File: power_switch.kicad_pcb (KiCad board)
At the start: 2 copper layers, 69 parts, among them P1 CONN_2, P10 CONN_2, P11 CONN_2, P12 CONN_2, P13 CONN_02X01, P2 CONN_2, P20 CONN_2, P3 CONN_2, P4 CONN_2, P5 CONN_2, P6 CONN_02X01, P7 CONN_02X01, P8 CONN_02X01, P9 CONN_2, Q1 2N7000, Q2 IRF9540, Q3 IRF9540, Q4 Q_NMOS_DGS, Q5 IRF9540, Q6 2N7000, U1 LM358

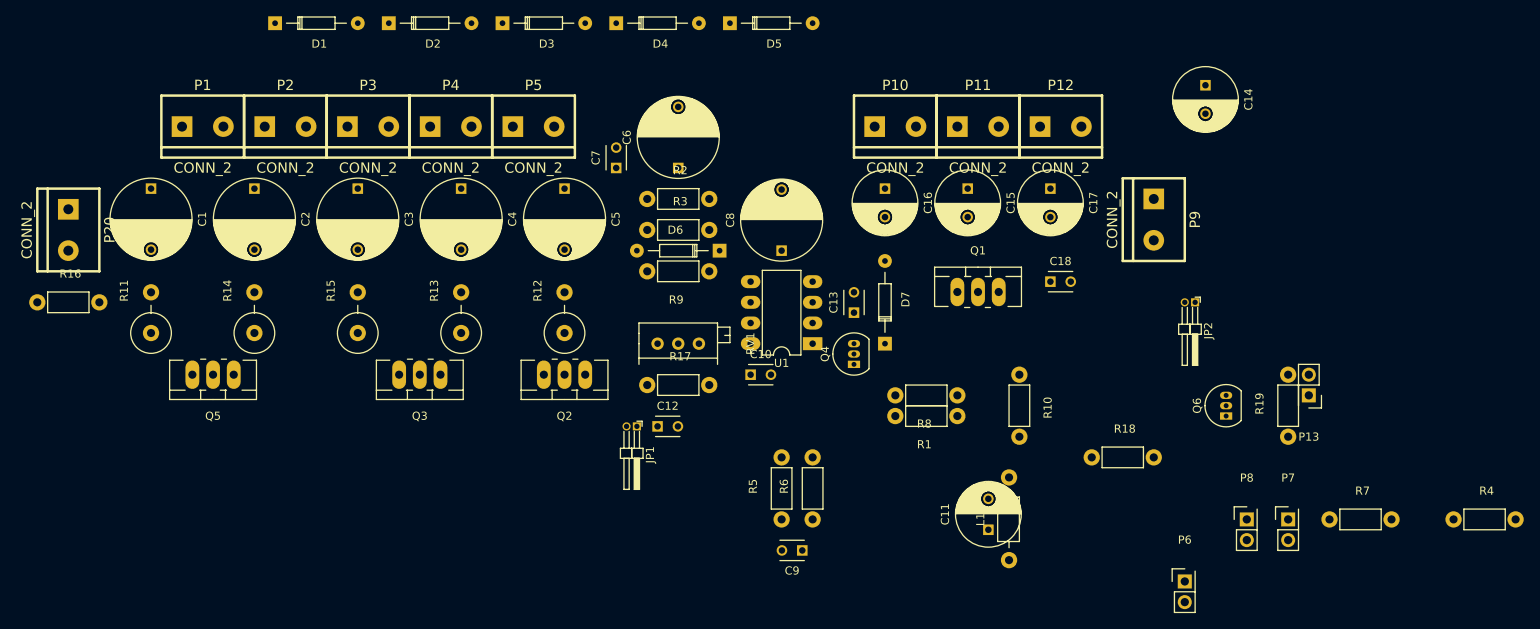
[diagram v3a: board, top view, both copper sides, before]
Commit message: powerswitch with tracks
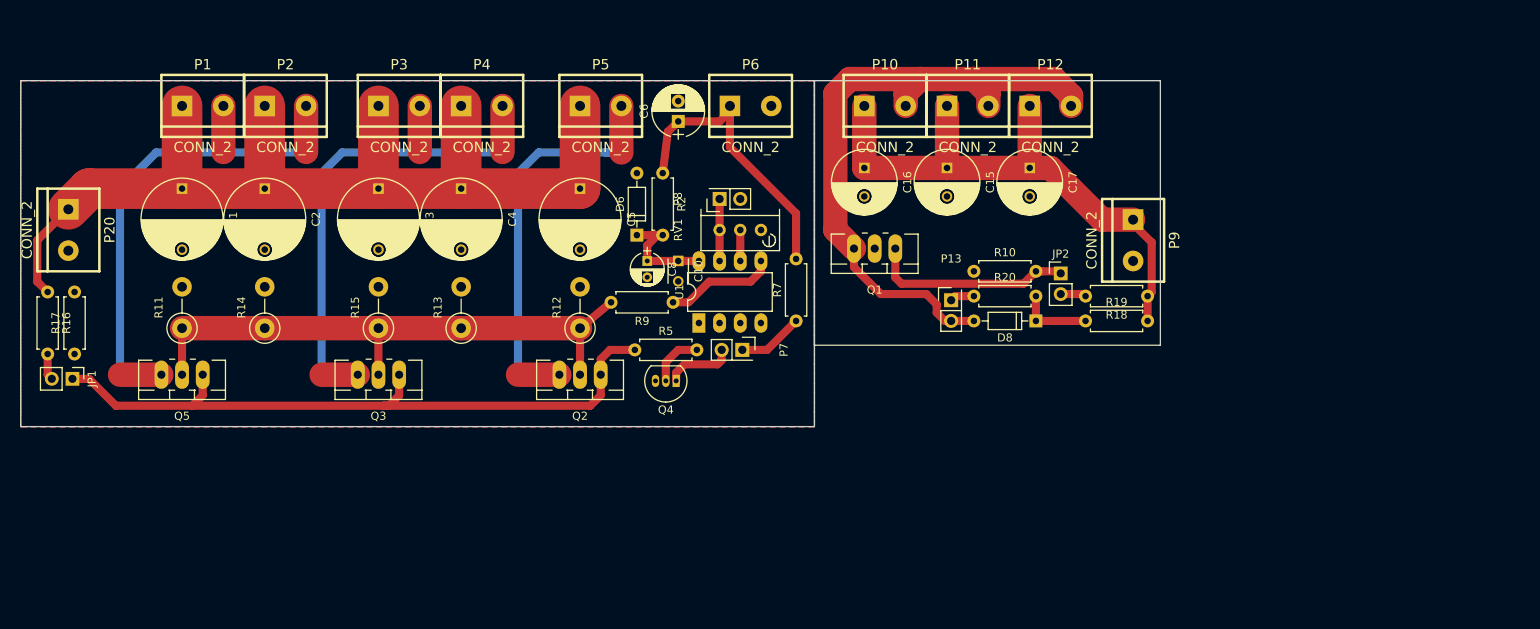
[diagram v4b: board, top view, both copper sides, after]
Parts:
- removed C11: 10uF, Capacitors_ThroughHole:C_Radial_D8_L13_P3.8
- removed C12, C18, C7, C9: 100n, Capacitors_ThroughHole:C_Disc_D3_P2.5
- removed C13: C, Capacitors_ThroughHole:C_Disc_D3_P2.5
- removed C14: 10uF, Capacitors_ThroughHole:C_Radial_D8_L11.5_P3.5
- removed D1, D2, D3, D4, D5: D, Diodes_ThroughHole:Diode_DO-35_SOD27_Horizontal_RM10
- removed D7: 1N4001, Diodes_ThroughHole:Diode_DO-35_SOD27_Horizontal_RM10
- removed L1: 50uH, Choke_Axial_ThroughHole:Choke_Horizontal_RM10mm
- removed Q6: 2N7000, TO_SOT_Packages_THT:TO-92_Inline_Narrow_Oval
- removed R1, R3, R6, R8: R, Resistors_ThroughHole:Resistor_Horizontal_RM7mm
- removed R4: 220R, Resistors_ThroughHole:Resistor_Horizontal_RM7mm
- added D8: 5v6, Diodes_ThroughHole:D_DO-35_SOD27_P7.62mm_Horizontal, F.Cu at (172.2, 64.5)
- added R20: 220R, Resistors_ThroughHole:R_Axial_DIN0207_L6.3mm_D2.5mm_P7.62mm_Horizontal, F.Cu at (164.6, 61.5)
- C6: footprint Capacitors_ThroughHole:C_Radial_D10_L20_P7.5 -> Capacitors_ThroughHole:CP_Radial_D6.3mm_P2.50mm
- C8: footprint Capacitors_ThroughHole:C_Radial_D10_L20_P7.5 -> Capacitors_ThroughHole:CP_Radial_D4.0mm_P2.00mm
- D6: footprint Diodes_ThroughHole:Diode_DO-35_SOD27_Horizontal_RM10 -> Diodes_ThroughHole:D_DO-35_SOD27_P7.62mm_Horizontal
- JP1, JP2: footprint Pin_Headers:Pin_Header_Angled_1x02_Pitch1.27mm -> Pin_Headers:Pin_Header_Straight_1x02_Pitch2.54mm
- P6: value CONN_02X01 -> CONN_2; footprint Socket_Strips:Socket_Strip_Straight_2x01 -> borniers:bornier2_V
- Q1: value 2N7000 -> IRF9540
- R10, R16, R17, R18, R19, R2, R5, R7, R9: footprint Resistors_ThroughHole:Resistor_Horizontal_RM7mm -> Resistors_ThroughHole:R_Axial_DIN0207_L6.3mm_D2.5mm_P7.62mm_Horizontal
- R11, R12, R13, R14, R15: footprint Resistors_ThroughHole:Resistor_Vertical_RM5mm -> Resistors_ThroughHole:R_Axial_DIN0411_L9.9mm_D3.6mm_P5.08mm_Vertical
- RV1: footprint Potentiometers:Potentiometer_Bourns_3296X_3-8Zoll_Inline_ScrewFront -> Potentiometers:Potentiometer_Bourns_3296W_3-8Zoll_Inline_ScrewUp
- moved P6 79.1 mm to (137.2, 38.1)
- moved P8 75.8 mm to (133.3, 49.5), turned to 90 degrees
- moved R17 70.5 mm to (54.1, 68.6), turned to 90 degrees
- moved P7 70.2 mm to (136.1, 68.1), turned to 270 degrees
- moved R7 69.9 mm to (142.7, 64.5), turned to 90 degrees
- moved JP1 69.6 mm to (53.8, 71.6)
- moved P13 45.5 mm to (161.8, 62.0), turned to 0 degrees
- moved R19 28.7 mm to (178.3, 64.5), turned to 0 degrees
- moved R5 27.6 mm to (122.9, 68.1), turned to 0 degrees
- moved Q4 21.9 mm to (128.0, 71.9), turned to 180 degrees
- moved R18 21.0 mm to (185.9, 61.5), turned to 180 degrees
- moved RV1 18.9 mm to (138.4, 53.3), turned to 90 degrees
- moved JP2 16.9 mm to (175.3, 58.7), turned to 0 degrees
- moved C8 16.6 mm to (124.5, 57.1), turned to 270 degrees
- moved C10 16.6 mm to (128.3, 57.1), turned to 270 degrees
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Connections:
- C6 pad 1: +36V -> +5V
- JP1 pad 1: Net-(JP1-Pad1) -> led1
- P10 pad 2: Net-(P10-Pad2) -> Net-(D8-Pad2)
- P11 pad 2: Net-(P10-Pad2) -> Net-(D8-Pad2)
- P12 pad 2: Net-(P10-Pad2) -> Net-(D8-Pad2)
- P13 pad 2: GNDA -> Net-(D8-Pad2)
- P6 pad 1: Net-(P6-Pad1) -> +5V
- P6 pad 2: Net-(P6-Pad2) -> GNDPWR
- P7 pad 2: GNDPWR -> Net-(P7-Pad2)
- Q1 pad 1: Net-(P6-Pad1) -> Net-(JP2-Pad1)
- Q1 pad 2: Net-(JP1-Pad1) -> GNDA
- Q1 pad 3: GNDPWR -> Net-(D8-Pad2)
- Q2 pad 1: Net-(JP1-Pad1) -> led1
- Q3 pad 1: Net-(JP1-Pad1) -> led1
- Q4 pad 1: +36V -> Net-(P7-Pad2)
- Q4 pad 3: Net-(D7-Pad1) -> GNDPWR
- Q5 pad 1: Net-(JP1-Pad1) -> led1
- R17 pad 1: Net-(JP1-Pad1) -> led1
- R19 pad 1: Net-(JP2-Pad1) -> Net-(D8-Pad1)
- R19 pad 2: Net-(P13-Pad1) -> +9V
- R2 pad 1: +36V -> +5V
- R5 pad 1: Net-(C10-Pad1) -> led1
- R5 pad 2: Net-(R1-Pad2) -> Net-(Q4-Pad2)
- U1 pad 1: Net-(Q4-Pad2) -> (no net)
- U1 pad 2: Net-(C13-Pad1) -> (no net)
- U1 pad 3: Net-(R1-Pad2) -> (no net)
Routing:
- net (no net): track 0.00 -> 134.8 mm
- net +36V: track 0.00 -> 127.6 mm
- net led1: track 0.00 -> 85.2 mm
- net Net-(D8-Pad2): track 0.00 -> 81.0 mm
- net +9V: track 0.00 -> 72.1 mm
- net Net-(Q2-Pad2): track 0.00 -> 71.0 mm
- net +5V: track 0.00 -> 36.0 mm
- net Net-(JP2-Pad1): track 0.00 -> 25.7 mm
- net Net-(P1-Pad2): track 0.00 -> 16.4 mm
- net Net-(P3-Pad2): track 0.00 -> 15.8 mm
- net Net-(C10-Pad1): track 0.00 -> 13.9 mm
- net Net-(C14-Pad1): track 0.00 -> 13.6 mm
- net Net-(P5-Pad2): track 0.00 -> 10.8 mm
- net Net-(D8-Pad1): track 0.00 -> 9.14 mm
- net Net-(P7-Pad2): track 0.00 -> 8.51 mm
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- added copper zone on F.Cu, net GNDPWR
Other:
- board outline added: 140 x 42.5 mm
- net class 9v added: clearance 0.1, trace_width 3, via_dia 0.6, via_drill 0.4
- net class Default: clearance 0.5 -> 0.1
- net class hp added: clearance 0.5, trace_width 5, via_dia 0.6, via_drill 0.4
- net class hp_return added: clearance 0.1, trace_width 3, via_dia 0.6, via_drill 0.4
- rule trace_clearance: 0.5 -> 0.1

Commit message: added pcb file
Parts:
- added REF**: MountingHole_3.2mm_M3, Mounting_Holes:MountingHole_3.2mm_M3, F.Cu at (145.8, 71.5)
- added REF**: MountingHole_3.2mm_M3, Mounting_Holes:MountingHole_3.2mm_M3, F.Cu at (183.8, 71.8)
- added REF**: MountingHole_3.2mm_M3, Mounting_Holes:MountingHole_3.2mm_M3, F.Cu at (156.5, 36.2)
- added REF**: MountingHole_3.2mm_M3, Mounting_Holes:MountingHole_3.2mm_M3, F.Cu at (55.2, 36.0)
- moved R18 29.6 mm to (159.0, 73.7), turned to 90 degrees
- moved P10 28.9 mm to (182.4, 41.5), turned to 270 degrees
- moved P9 25.2 mm to (165.9, 72.0), turned to 180 degrees
- moved P12 25.2 mm to (182.4, 61.8), turned to 270 degrees
- moved C16 24.6 mm to (174.8, 39.0), turned to 180 degrees
- moved P11 23.0 mm to (182.4, 51.6), turned to 270 degrees
- moved R19 22.4 mm to (156.0, 66.1), turned to 270 degrees
- moved Q1 19.8 mm to (164.9, 40.2), turned to 90 degrees
- moved D8 16.8 mm to (156.0, 60.0), turned to 90 degrees
- moved JP2 14.1 mm to (161.8, 63.1), turned to 270 degrees
- moved C17 14.0 mm to (174.8, 59.3), turned to 180 degrees
- moved C15 13.9 mm to (174.8, 49.1), turned to 180 degrees
- moved P13 12.8 mm to (158.5, 49.6), turned to 270 degrees
- moved R20 10.6 mm to (159.0, 52.4), turned to 270 degrees
- moved R10 6.51 mm to (162.1, 52.4), turned to 270 degrees
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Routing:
- added copper zone on F.Cu, net GNDA
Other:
- board size 140 x 42.5 mm -> 135.8 x 42.8 mm

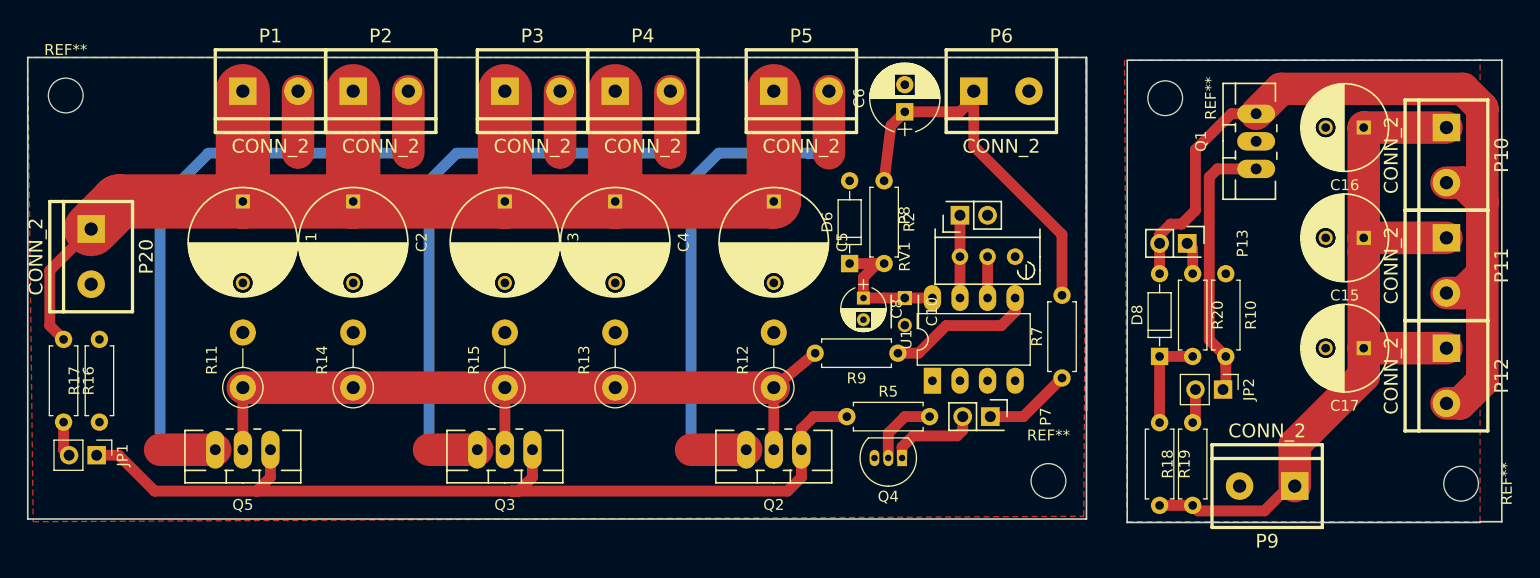
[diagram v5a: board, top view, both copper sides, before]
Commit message: corrected switching transistor pins order
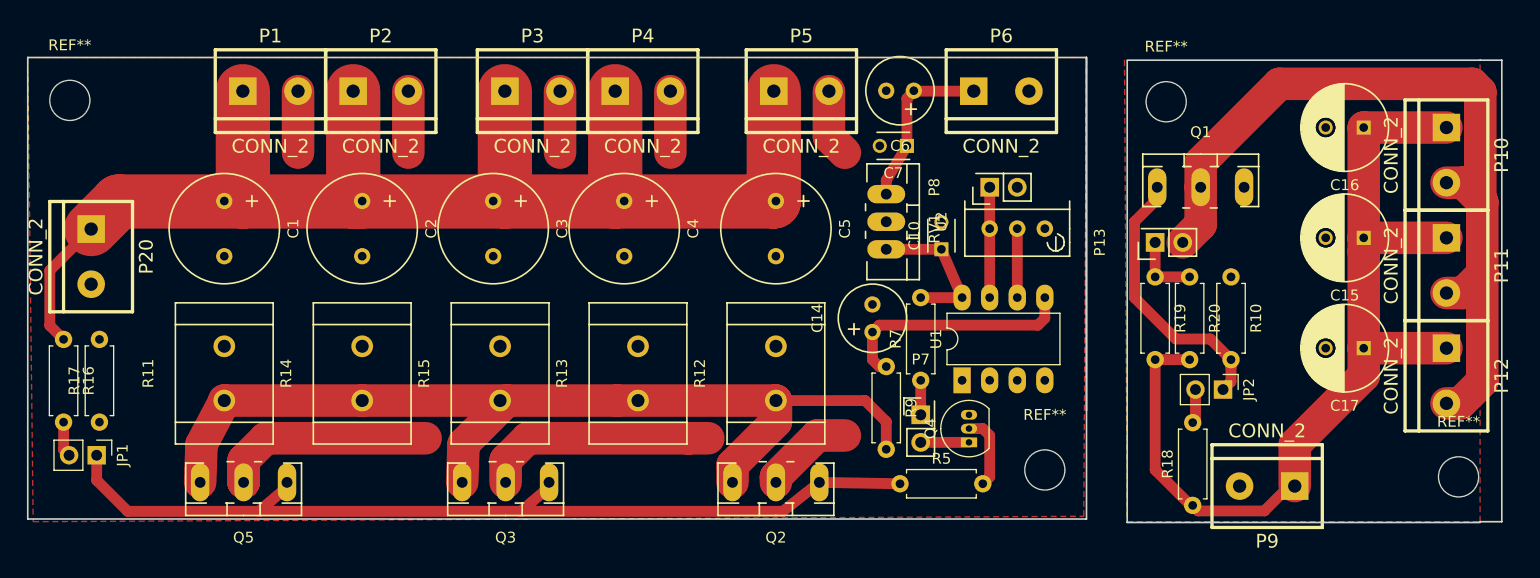
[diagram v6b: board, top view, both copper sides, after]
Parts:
- removed C8: 10uF, Capacitors_ThroughHole:CP_Radial_D4.0mm_P2.00mm
- removed D6, D8: 5v6, Diodes_ThroughHole:D_DO-35_SOD27_P7.62mm_Horizontal
- removed R2: R, Resistors_ThroughHole:R_Axial_DIN0207_L6.3mm_D2.5mm_P7.62mm_Horizontal
- removed the REF** at (145.8, 71.5)
- removed the REF** at (183.8, 71.8)
- removed the REF** at (156.5, 36.2)
- removed the REF** at (55.2, 36.0)
- added C14: 10uF, Capacitors_Elko_ThroughHole:Elko_vert_11.2x6.3mm_RM2.5, F.Cu at (129.5, 57.8)
- added C7: 100n, Capacitors_ThroughHole:C_Disc_D3_P2.5, F.Cu at (132.7, 40.6)
- added REF**: MountingHole_3-7mm, Mounting_Holes:MountingHole_3-7mm, F.Cu at (145.4, 70.5)
- added REF**: MountingHole_3-7mm, Mounting_Holes:MountingHole_3-7mm, F.Cu at (55.6, 36.4)
- added REF**: MountingHole_3-7mm, Mounting_Holes:MountingHole_3-7mm, F.Cu at (183.5, 71.1)
- added REF**: MountingHole_3-7mm, Mounting_Holes:MountingHole_3-7mm, F.Cu at (156.6, 36.6)
- added U2: LM7805, Transistors_TO-220:TO-220_L78XX, F.Cu at (130.8, 47.6)
- C1, C2, C3, C4, C5: footprint Capacitors_ThroughHole:C_Radial_D10_L20_P7.5 -> Capacitors_Elko_ThroughHole:Elko_vert_20x10mm_RM5
- C6: footprint Capacitors_ThroughHole:CP_Radial_D6.3mm_P2.50mm -> Capacitors_Elko_ThroughHole:Elko_vert_11.2x6.3mm_RM2.5
- Q1, Q2, Q3, Q5: footprint TO_SOT_Packages_THT:TO-220_Neutral123_Vertical_LargePads -> Transistors_TO-220:TO-220_Neutral123_Vertical_LargePads_wide
- R11, R12, R13, R14, R15: footprint Resistors_ThroughHole:R_Axial_DIN0411_L9.9mm_D3.6mm_P5.08mm_Vertical -> Resistors_ThroughHole:Resistor_Cement_KOA-BGR-3N
- moved R19 13.4 mm to (155.6, 52.7)
- moved R7 13.0 mm to (134.0, 62.2)
- moved R5 7.89 mm to (132.1, 71.8)
- moved Q1 6.63 mm to (159.8, 44.5), turned to 0 degrees
- moved P7 6.41 mm to (134.0, 65.4), turned to 0 degrees
- moved Q4 6.33 mm to (138.4, 67.9), turned to 90 degrees
- moved C10 5.61 mm to (135.9, 50.2), turned to 90 degrees
- moved P8 3.76 mm to (140.3, 44.5)
- moved RV1 3.76 mm to (145.4, 48.3)
- moved Q2 3.01 mm to (120.7, 71.6)
- moved Q3 3.01 mm to (95.8, 71.6)
- moved Q5 3.01 mm to (71.6, 71.6)
- moved P13 2.95 mm to (155.6, 49.5), turned to 90 degrees
- moved U1 2.74 mm to (137.8, 62.2)
- moved R13 2.48 mm to (108.0, 61.6)
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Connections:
- C10 pad 1: Net-(C10-Pad1) -> +5V
- C6 pad 1: +5V -> +12V
- P10 pad 2: Net-(D8-Pad2) -> Net-(P10-Pad2)
- P11 pad 2: Net-(D8-Pad2) -> Net-(P10-Pad2)
- P12 pad 2: Net-(D8-Pad2) -> Net-(P10-Pad2)
- P13 pad 2: Net-(D8-Pad2) -> Net-(P10-Pad2)
- P6 pad 1: +5V -> +12V
- Q1 pad 2: GNDA -> Net-(P10-Pad2)
- Q1 pad 3: Net-(D8-Pad2) -> GNDA
- Q2 pad 2: Net-(Q2-Pad2) -> Net-(P5-Pad2)
- Q2 pad 3: Net-(P5-Pad2) -> Net-(Q2-Pad3)
- Q3 pad 2: Net-(Q2-Pad2) -> Net-(P3-Pad2)
- Q3 pad 3: Net-(P3-Pad2) -> Net-(Q2-Pad3)
- Q5 pad 2: Net-(Q2-Pad2) -> Net-(P1-Pad2)
- Q5 pad 3: Net-(P1-Pad2) -> Net-(Q2-Pad3)
- R11 pad 1: Net-(Q2-Pad2) -> Net-(Q2-Pad3)
- R12 pad 1: Net-(Q2-Pad2) -> Net-(Q2-Pad3)
- R13 pad 1: Net-(Q2-Pad2) -> Net-(Q2-Pad3)
- R14 pad 1: Net-(Q2-Pad2) -> Net-(Q2-Pad3)
- R15 pad 1: Net-(Q2-Pad2) -> Net-(Q2-Pad3)
- R19 pad 1: Net-(D8-Pad1) -> Net-(P13-Pad1)
- R20 pad 2: Net-(D8-Pad1) -> +9V
- R9 pad 2: Net-(Q2-Pad2) -> Net-(Q2-Pad3)
- U1 pad 8: Net-(C10-Pad1) -> +5V
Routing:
- net (no net): track 134.8 -> 0.00 mm
- net Net-(Q2-Pad3): track 0.00 -> 90.8 mm
- net Net-(D8-Pad2): track 81.0 -> 0.00 mm
- net Net-(P10-Pad2): track 0.00 -> 75.8 mm
- net Net-(Q2-Pad2): track 71.0 -> 0.00 mm
- net +5V: track 36.0 -> 13.7 mm
- net Net-(P1-Pad2): track 16.4 -> 33.9 mm
- net Net-(P3-Pad2): track 15.8 -> 33.0 mm
- net +12V: track 0.00 -> 16.4 mm
- net +9V: track 72.1 -> 87.2 mm
- net Net-(C10-Pad1): track 13.9 -> 0.00 mm
- net Net-(D8-Pad1): track 9.14 -> 0.00 mm
- net Net-(C14-Pad1): track 13.6 -> 22.4 mm
- net Net-(P7-Pad1): track 8.08 -> 3.18 mm
- net Net-(P7-Pad2): track 8.51 -> 4.44 mm
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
